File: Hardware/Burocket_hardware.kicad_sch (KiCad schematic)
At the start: 0 parts

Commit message: Added a simulations file, added App Notes file, Finalized SD-card design type shit
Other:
- note added: "TODO: - Add buzzer Consider piezo for lower electrical noise. - Finish power schematics. - Finish SD-card schematics - Finish USB schematics - Additionally read USB-c VBUS voltage"
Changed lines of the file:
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@@
 		(company "Burocket")
+	)
+	(text "TODO:\n- Add buzzer \nConsider piezo for lower electrical noise.\n- Finish power schematics.\n- Finish SD-card schematics\n- Finish USB schematics\n- Additionally read USB-c VBUS voltage"
+		(exclude_from_sim no)
+		(at -163.195 9.525 0)
+		(effects
+			(font
+				(size 5.08 5.08)
+				(thickness 1.016)
+				(bold yes)
+			)
+			(justify left)
+		)
 	)
 	(sheet

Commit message: +1000 Aura
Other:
- note added: "TODO: - Add buzzer. - Finish power schematics. - Additionally read USB-c VBUS voltage. - Add Lora Module footprint"
- note removed: "TODO: - Add buzzer Consider piezo for lower electrical noise. - Finish power schematics. - Finish SD-card schematics - Finish USB schematics - Additionally read USB-c VBUS voltage"
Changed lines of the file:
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@@
 		(company "Burocket")
 	)
-	(text "TODO:\n- Add buzzer \nConsider piezo for lower electrical noise.\n- Finish power schematics.\n- Finish SD-card schematics\n- Finish USB schematics\n- Additionally read USB-c VBUS voltage"
+	(text "TODO:\n- Add buzzer.\n- Finish power schematics.\n- Additionally read USB-c VBUS voltage.\n- Add Lora Module footprint"
 		(exclude_from_sim no)
 		(at -163.195 9.525 0)

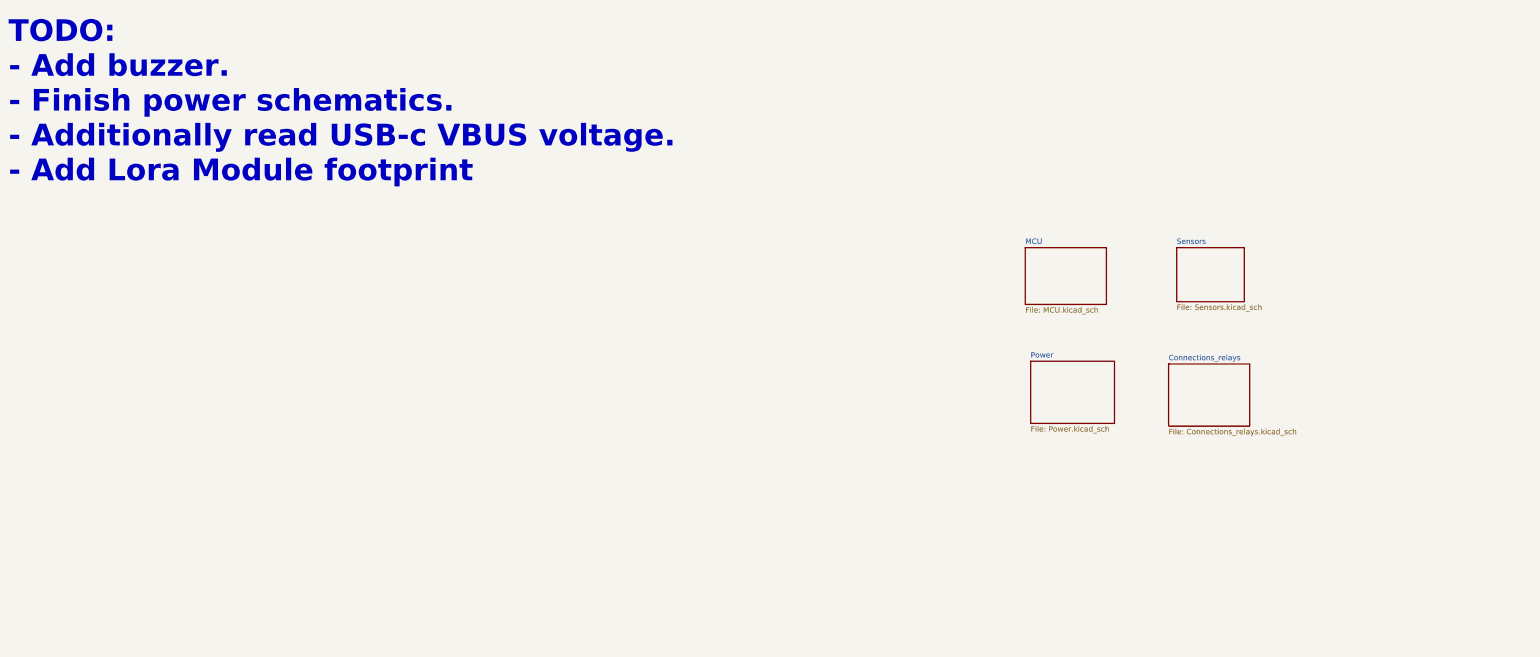
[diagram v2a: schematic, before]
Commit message: Only SSR and ferrite bead selection is left
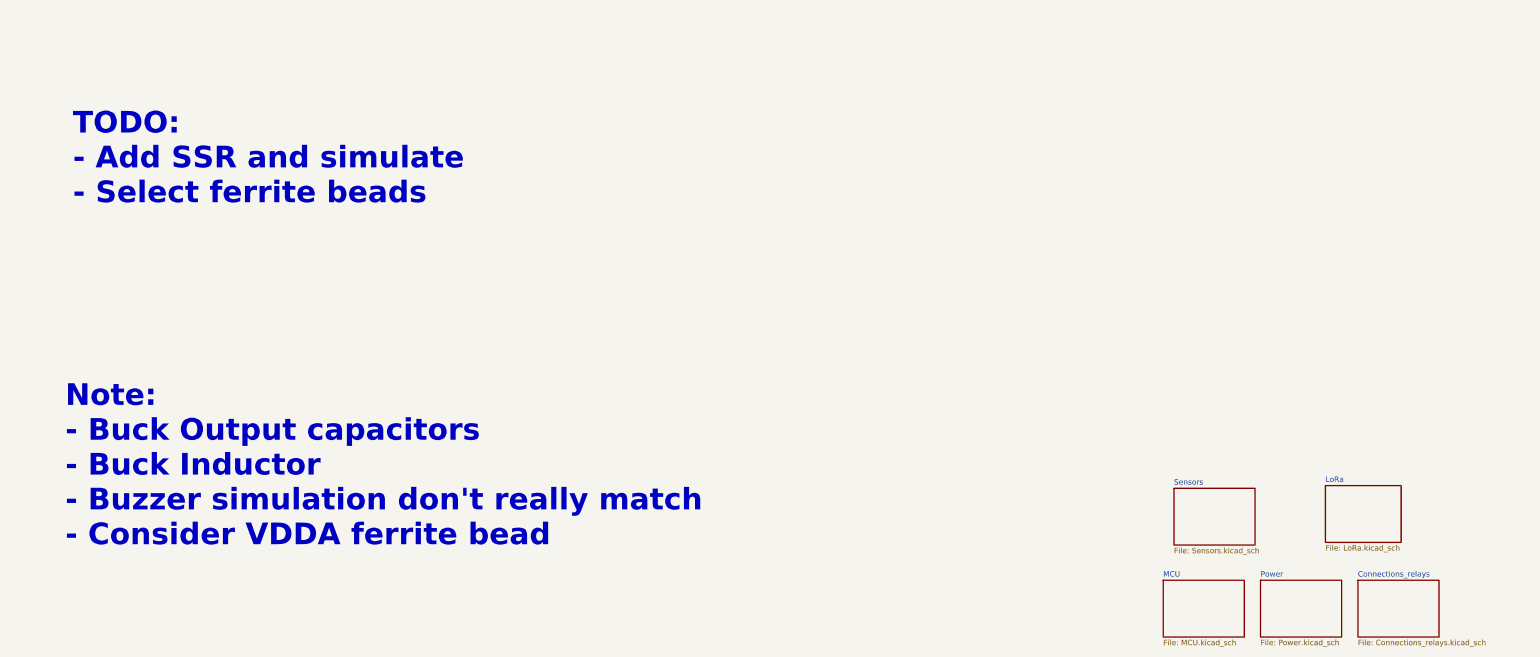
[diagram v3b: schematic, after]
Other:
- added sheet LoRa (LoRa.kicad_sch)
- note added: "Note: - Buck Output capacitors - Buck Inductor - Buzzer simulation don't really match - Consider VDDA ferrite bead"
- note added: "TODO: - Add SSR and simulate - Select ferrite beads"
- note removed: "TODO: - Add buzzer. - Finish power schematics. - Additionally read USB-c VBUS voltage. - Add Lora Module footprint"
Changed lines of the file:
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@@
 		(company "Burocket")
 	)
-	(text "TODO:\n- Add buzzer.\n- Finish power schematics.\n- Additionally read USB-c VBUS voltage.\n- Add Lora Module footprint"
-		(exclude_from_sim no)
-		(at -163.195 9.525 0)
+	(text "TODO:\n- Add SSR and simulate\n- Select ferrite beads"
+		(exclude_from_sim no)
+		(at -148.082 22.86 0)
 		(effects
 			(font
@@
 		)
 	)
-	(sheet
-		(at 109.22 71.12)
-		(size 19.05 14.605)
+	(text "Note:\n- Buck Output capacitors\n- Buck Inductor\n- Buzzer simulation don't really match \n- Consider VDDA ferrite bead"
+		(exclude_from_sim no)
+		(at -149.86 94.996 0)
+		(effects
+			(font
+				(size 5.08 5.08)
+				(thickness 1.016)
+				(bold yes)
+			)
+			(justify left)
+		)
+	)
+	(sheet
+		(at 153.67 121.92)
+		(size 19.05 13.335)
 		(exclude_from_sim no)
 		(in_bom yes)
@@
 		)
 		(property "Sheetname" "Connections_relays"
-			(at 109.22 70.4084 0)
+			(at 153.67 121.2084 0)
 			(show_name no)
 			(do_not_autoplace no)
@@
 		)
 		(property "Sheetfile" "Connections_relays.kicad_sch"
-			(at 109.22 86.3096 0)
+			(at 153.67 135.8396 0)
 			(show_name no)
 			(do_not_autoplace no)
@@
 	)
 	(sheet
-		(at 111.125 43.815)
-		(size 15.875 12.7)
+		(at 110.49 100.33)
+		(size 19.05 13.335)
 		(exclude_from_sim no)
 		(in_bom yes)
@@
 		)
 		(property "Sheetname" "Sensors"
-			(at 111.125 43.1034 0)
+			(at 110.49 99.6184 0)
 			(show_name no)
 			(do_not_autoplace no)
@@
 		)
 		(property "Sheetfile" "Sensors.kicad_sch"
-			(at 111.125 57.0996 0)
+			(at 110.49 114.2496 0)
 			(show_name no)
 			(do_not_autoplace no)
@@
 	)
 	(sheet
-		(at 76.835 70.485)
-		(size 19.685 14.605)
+		(at 130.81 121.92)
+		(size 19.05 13.335)
 		(exclude_from_sim no)
 		(in_bom yes)
@@
 		)
 		(property "Sheetname" "Power"
-			(at 76.835 69.7734 0)
+			(at 130.81 121.2084 0)
 			(show_name no)
 			(do_not_autoplace no)
@@
 		)
 		(property "Sheetfile" "Power.kicad_sch"
-			(at 76.835 85.6746 0)
+			(at 130.81 135.8396 0)
 			(show_name no)
 			(do_not_autoplace no)
@@
 	)
 	(sheet
-		(at 75.565 43.815)
+		(at 107.95 121.92)
 		(size 19.05 13.335)
 		(exclude_from_sim no)
@@
 		)
 		(property "Sheetname" "MCU"
-			(at 75.565 43.1034 0)
+			(at 107.95 121.2084 0)
 			(show_name no)
 			(do_not_autoplace no)
@@
 		)
 		(property "Sheetfile" "MCU.kicad_sch"
-			(at 75.565 57.7346 0)
+			(at 107.95 135.8396 0)
 			(show_name no)
 			(do_not_autoplace no)
@@
 				)
 			)
+		)
+	)
+	(sheet
+		(at 146.05 99.695)
+		(size 17.78 13.335)
+		(exclude_from_sim no)
+		(in_bom yes)
+		(on_board yes)
+		(dnp no)
+		(fields_autoplaced yes)
+		(stroke
+			(width 0.1524)
+			(type solid)
+		)
+		(fill
+			(color 0 0 0 0)
+		)
+		(property "Sheetname" "LoRa"
+			(at 146.05 98.9834 0)
+			(show_name no)
+			(do_not_autoplace no)
+			(effects
+				(font
+					(size 1.27 1.27)
+				)
+				(justify left bottom)
+			)
+		)
+		(property "Sheetfile" "LoRa.kicad_sch"
+			(at 146.05 113.6146 0)
+			(show_name no)
+			(do_not_autoplace no)
+			(effects
+				(font
+					(size 1.27 1.27)
+				)
+				(justify left top)
+			)
+		)
+		(instances
+			(project "Burocket_hardware"
+				(path "/ece13985-822e-4117-ba82-38a772aa2f0c"
+					(page "6")
+				)
+			)

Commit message: Ne yazacagimi bilemedim
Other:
- note added: "TODO: - Select caps for the Buck converter - Add SSR and simulate - Select ferrite beads - Add current sense amplifier with a shunt resistor - Complete sensor page - Complete LoRa page"
- note removed: "TODO: - Add SSR and simulate - Select ferrite beads"
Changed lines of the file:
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@@
 		(company "Burocket")
 	)
-	(text "TODO:\n- Add SSR and simulate\n- Select ferrite beads"
-		(exclude_from_sim no)
-		(at -148.082 22.86 0)
+	(text "TODO:\n- Select caps for the Buck converter\n- Add SSR and simulate\n- Select ferrite beads\n- Add current sense amplifier \nwith a shunt resistor\n- Complete sensor page\n- Complete LoRa page"
+		(exclude_from_sim no)
+		(at -163.576 72.39 0)
 		(effects
 			(font
@@
 	(text "Note:\n- Buck Output capacitors\n- Buck Inductor\n- Buzzer simulation don't really match \n- Consider VDDA ferrite bead"
 		(exclude_from_sim no)
-		(at -149.86 94.996 0)
+		(at -163.576 128.778 0)
 		(effects
 			(font
@@
 	)
 	(sheet
-		(at 153.67 121.92)
+		(at 136.144 74.93)
+		(size 18.288 14.478)
+		(exclude_from_sim no)
+		(in_bom yes)
+		(on_board yes)
+		(dnp no)
+		(fields_autoplaced yes)
+		(stroke
+			(width 0.1524)
+			(type solid)
+		)
+		(fill
+			(color 0 0 0 0)
+		)
+		(property "Sheetname" "Connections_relays"
+			(at 136.144 74.2184 0)
+			(show_name no)
+			(do_not_autoplace no)
+			(effects
+				(font
+					(size 1.27 1.27)
+				)
+				(justify left bottom)
+			)
+		)
+		(property "Sheetfile" "Connections_relays.kicad_sch"
+			(at 136.144 89.9926 0)
+			(show_name no)
+			(do_not_autoplace no)
+			(effects
+				(font
+					(size 1.27 1.27)
+				)
+				(justify left top)
+			)
+		)
+		(instances
+			(project "Burocket_hardware"
+				(path "/ece13985-822e-4117-ba82-38a772aa2f0c"
+					(page "5")
+				)
+			)
+		)
+	)
+	(sheet
+		(at 137.16 98.806)
 		(size 19.05 13.335)
 		(exclude_from_sim no)
@@
 			(color 0 0 0 0)
 		)
-		(property "Sheetname" "Connections_relays"
-			(at 153.67 121.2084 0)
-			(show_name no)
-			(do_not_autoplace no)
-			(effects
-				(font
-					(size 1.27 1.27)
-				)
-				(justify left bottom)
-			)
-		)
-		(property "Sheetfile" "Connections_relays.kicad_sch"
-			(at 153.67 135.8396 0)
-			(show_name no)
-			(do_not_autoplace no)
-			(effects
-				(font
-					(size 1.27 1.27)
-				)
-				(justify left top)
-			)
-		)
-		(instances
-			(project "Burocket_hardware"
-				(path "/ece13985-822e-4117-ba82-38a772aa2f0c"
-					(page "5")
-				)
-			)
-		)
-	)
-	(sheet
-		(at 110.49 100.33)
+		(property "Sheetname" "Sensors"
+			(at 137.16 98.0944 0)
+			(show_name no)
+			(do_not_autoplace no)
+			(effects
+				(font
+					(size 1.27 1.27)
+				)
+				(justify left bottom)
+			)
+		)
+		(property "Sheetfile" "Sensors.kicad_sch"
+			(at 137.16 112.7256 0)
+			(show_name no)
+			(do_not_autoplace no)
+			(effects
+				(font
+					(size 1.27 1.27)
+				)
+				(justify left top)
+			)
+		)
+		(instances
+			(project "Burocket_hardware"
+				(path "/ece13985-822e-4117-ba82-38a772aa2f0c"
+					(page "3")
+				)
+			)
+		)
+	)
+	(sheet
+		(at 112.268 98.806)
 		(size 19.05 13.335)
 		(exclude_from_sim no)
@@
 			(color 0 0 0 0)
 		)
-		(property "Sheetname" "Sensors"
-			(at 110.49 99.6184 0)
-			(show_name no)
-			(do_not_autoplace no)
-			(effects
-				(font
-					(size 1.27 1.27)
-				)
-				(justify left bottom)
-			)
-		)
-		(property "Sheetfile" "Sensors.kicad_sch"
-			(at 110.49 114.2496 0)
-			(show_name no)
-			(do_not_autoplace no)
-			(effects
-				(font
-					(size 1.27 1.27)
-				)
-				(justify left top)
-			)
-		)
-		(instances
-			(project "Burocket_hardware"
-				(path "/ece13985-822e-4117-ba82-38a772aa2f0c"
-					(page "3")
-				)
-			)
-		)
-	)
-	(sheet
-		(at 130.81 121.92)
-		(size 19.05 13.335)
-		(exclude_from_sim no)
-		(in_bom yes)
-		(on_board yes)
-		(dnp no)
-		(fields_autoplaced yes)
-		(stroke
-			(width 0.1524)
-			(type solid)
-		)
-		(fill
-			(color 0 0 0 0)
-		)
 		(property "Sheetname" "Power"
-			(at 130.81 121.2084 0)
+			(at 112.268 98.0944 0)
 			(show_name no)
 			(do_not_autoplace no)
@@
 		)
 		(property "Sheetfile" "Power.kicad_sch"
-			(at 130.81 135.8396 0)
+			(at 112.268 112.7256 0)
 			(show_name no)
 			(do_not_autoplace no)
@@
 	)
 	(sheet
-		(at 107.95 121.92)
-		(size 19.05 13.335)
+		(at 112.776 73.914)
+		(size 20.066 16.002)
 		(exclude_from_sim no)
 		(in_bom yes)
@@
 		)
 		(property "Sheetname" "MCU"
-			(at 107.95 121.2084 0)
+			(at 112.776 73.2024 0)
 			(show_name no)
 			(do_not_autoplace no)
@@
 		)
 		(property "Sheetfile" "MCU.kicad_sch"
-			(at 107.95 135.8396 0)
+			(at 112.776 90.5006 0)
 			(show_name no)
 			(do_not_autoplace no)
@@
 	)
 	(sheet
-		(at 146.05 99.695)
+		(at 160.02 98.679)
 		(size 17.78 13.335)
 		(exclude_from_sim no)
@@
 		)
 		(property "Sheetname" "LoRa"
-			(at 146.05 98.9834 0)
+			(at 160.02 97.9674 0)
 			(show_name no)
 			(do_not_autoplace no)
@@
 		)
 		(property "Sheetfile" "LoRa.kicad_sch"
-			(at 146.05 113.6146 0)
-			(show_name no)
-			(do_not_autoplace no)
+			(at 160.02 112.5986 0)
+			(show_name no)
+			(do_not_autoplace no)

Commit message: Commit bulamadim :)
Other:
- note added: "TODO: - Consider changing the X6S caps - Consider series resisrance on UART and SPI lines - Check if open-drain and interrupt pin is valid - Consider another inductor for the buck converter - Select ferrite beads - Consider pull-up resistor values on I2C - Consider Passive components - Consider and thoroughly check all footprints - Check if STM32CubeMX matches the MCU page - Check all footprints 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"
- note removed: "TODO: - Select caps for the Buck converter - Add SSR and simulate - Select ferrite beads - Add current sense amplifier with a shunt resistor - Complete sensor page - Complete LoRa page"
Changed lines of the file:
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@@
 		(company "Burocket")
 	)
-	(text "TODO:\n- Select caps for the Buck converter\n- Add SSR and simulate\n- Select ferrite beads\n- Add current sense amplifier \nwith a shunt resistor\n- Complete sensor page\n- Complete LoRa page"
+	(text "TODO:\n- Consider changing the X6S caps\n- Consider series resisrance on UART and SPI lines\n- Check if open-drain and interrupt pin is valid\n- Consider another inductor for the buck converter\n- Select ferrite beads\n- Consider pull-up resistor values on I2C\n- Consider Passive components\n- Consider and thoroughly check all footprints\n- Check if STM32CubeMX matches the MCU page\n- Check all footprints\n- Add tables to schematics for better explanation\n\n\n- Select caps for the Buck converter\n- Add SSR and simulate"
 		(exclude_from_sim no)
-		(at -163.576 72.39 0)
+		(at -215.138 51.562 0)
 		(effects
 			(font
@@
 	(text "Note:\n- Buck Output capacitors\n- Buck Inductor\n- Buzzer simulation don't really match \n- Consider VDDA ferrite bead"
 		(exclude_from_sim no)
-		(at -163.576 128.778 0)
+		(at -216.916 175.26 0)
 		(effects
 			(font

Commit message: Added New file for additional resources used, Changed LDO for lower noise, changed buck converter for higher switching speed, smaller inductance value, better transient current response
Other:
- added sheet USB-c (USB-c.kicad_sch)
- note added: "TODO: - Complete buck converter circuit - Complete SSR circuit - Complete Buzzer circuit - Select ferrite beads - Consider Passive components - Consider and thoroughly check all footprints - Select caps for the Buck converter - Add SSR and simulate"
- note removed: "TODO: - Consider changing the X6S caps - Consider series resisrance on UART and SPI lines - Check if open-drain and interrupt pin is valid - Consider another inductor for the buck converter - Select ferrite beads - Consider pull-up resistor values on I2C - Consider Passive components - Consider and thoroughly check all footprints - Check if STM32CubeMX matches the MCU page - Check all footprints 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"
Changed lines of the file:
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@@
 		(company "Burocket")
 	)
-	(text "TODO:\n- Consider changing the X6S caps\n- Consider series resisrance on UART and SPI lines\n- Check if open-drain and interrupt pin is valid\n- Consider another inductor for the buck converter\n- Select ferrite beads\n- Consider pull-up resistor values on I2C\n- Consider Passive components\n- Consider and thoroughly check all footprints\n- Check if STM32CubeMX matches the MCU page\n- Check all footprints\n- Add tables to schematics for better explanation\n\n\n- Select caps for the Buck converter\n- Add SSR and simulate"
-		(exclude_from_sim no)
-		(at -215.138 51.562 0)
+	(text "TODO:\n- Complete buck converter circuit\n- Complete SSR circuit\n- Complete Buzzer circuit\n- Select ferrite beads\n- Consider Passive components\n\n\n- Consider and thoroughly check all footprints\n- Select caps for the Buck converter\n- Add SSR and simulate"
+		(exclude_from_sim no)
+		(at -211.582 50.038 0)
 		(effects
 			(font
@@
 	(text "Note:\n- Buck Output capacitors\n- Buck Inductor\n- Buzzer simulation don't really match \n- Consider VDDA ferrite bead"
 		(exclude_from_sim no)
-		(at -216.916 175.26 0)
+		(at -215.138 147.574 0)
 		(effects
 			(font
@@
 				)
 			)
+		)
+	)
+	(sheet
+		(at 160.274 74.676)
+		(size 19.558 13.462)
+		(exclude_from_sim no)
+		(in_bom yes)
+		(on_board yes)
+		(dnp no)
+		(fields_autoplaced yes)
+		(stroke
+			(width 0.1524)
+			(type solid)
+		)
+		(fill
+			(color 0 0 0 0)
+		)
+		(property "Sheetname" "USB-c"
+			(at 160.274 73.9644 0)
+			(show_name no)
+			(do_not_autoplace no)
+			(effects
+				(font
+					(size 1.27 1.27)
+				)
+				(justify left bottom)
+			)
+		)
+		(property "Sheetfile" "USB-c.kicad_sch"
+			(at 160.274 88.7226 0)
+			(show_name no)
+			(do_not_autoplace no)
+			(effects
+				(font
+					(size 1.27 1.27)
+				)
+				(justify left top)
+			)
+		)
+		(instances
+			(project "Burocket_hardware"
+				(path "/ece13985-822e-4117-ba82-38a772aa2f0c"
+					(page "7")
+				)
+			)

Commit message: Added Impedance matching calculations, finished buck converter calculations, finalized buzzer circuitry
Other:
- note added: "Note: - Buzzer simulation don't really match"
- note added: "TODO: - Must change nmos driving E-match - Consider Passive components - Consider and thoroughly check all footprints"
- note removed: "Note: - Buck Output capacitors - Buck Inductor - Buzzer simulation don't really match - Consider VDDA ferrite bead"
- note removed: "TODO: - Complete buck converter circuit - Complete SSR circuit - Complete Buzzer circuit - Select ferrite beads - Consider Passive components - Consider and thoroughly check all footprints - Select caps for the Buck converter - Add SSR and simulate"
